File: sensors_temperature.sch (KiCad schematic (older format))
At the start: 3 parts

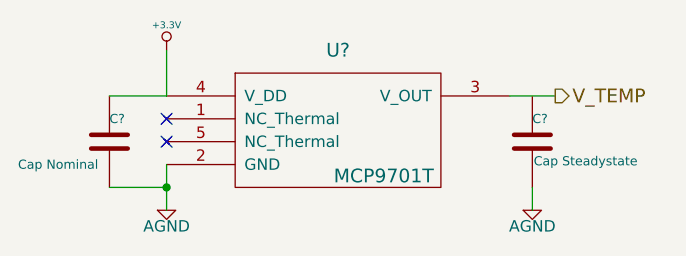
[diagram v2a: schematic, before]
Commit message: various fixes due to issues found in ERC
learned how to use invisible pins
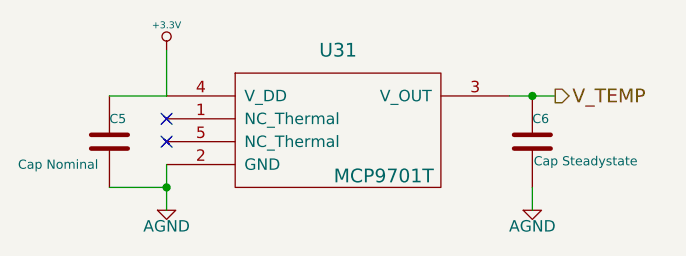
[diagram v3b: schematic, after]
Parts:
- gave numbers to parts that had none: 3
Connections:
- net V_TEMP: now also C6.1
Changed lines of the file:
@@
 $Descr A4 11693 8268
 encoding utf-8
-Sheet 9 18
+Sheet 7 18
 Title ""
-Date "18 dec 2013"
+Date "20 dec 2013"
 Rev ""
 Comp ""
@@
 $EndDescr
 $Comp
-L C C?
+L C C5
 U 1 1 5279CE8C
 P 1050 1250
-F 0 "C?" H 1050 1350 40  0000 L CNN
+F 0 "C5" H 1050 1350 40  0000 L CNN
 F 1 "Cap Nominal" H 650 1150 40  0000 L CNN
 F 2 "~" H 1088 1100 30  0000 C CNN
@@
 $EndComp
 $Comp
-L MCP9701T U?
+L MCP9701T U31
 U 1 1 5279CF6F
 P 2100 1250
-F 0 "U?" H 2050 1650 60  0000 C CNN
+F 0 "U31" H 2050 1650 60  0000 C CNN
 F 1 "MCP9701T" H 2250 1100 60  0000 C CNN
 F 2 "" H 1800 1650 60  0000 C CNN
@@
 $EndComp
 $Comp
-L +3.3V #PWR?
+L +3.3V #PWR039
 U 1 1 5279CF8D
 P 1300 850
-F 0 "#PWR?" H 1300 810 30  0001 C CNN
+F 0 "#PWR039" H 1300 810 30  0001 C CNN
 F 1 "+3.3V" H 1300 960 30  0000 C CNN
 F 2 "" H 1300 850 60  0000 C CNN
@@
 NoConn ~ 1300 1150
 NoConn ~ 1300 1250
-Wire Wire Line
-	2800 1050 3000 1050
 Connection ~ 1300 1450
 Wire Wire Line
@@
 	1300 1050 1050 1050
 Wire Wire Line
-	1300 1350 1300 1450
-Wire Wire Line
-	1300 1450 1300 1550
+	1300 1350 1300 1550
 Wire Wire Line
 	1300 850  1300 1050
@@
 	2900 1550 2900 1450
 $Comp
-L C C?
+L C C6
 U 1 1 527B2035
 P 2900 1250
-F 0 "C?" H 2900 1350 40  0000 L CNN
+F 0 "C6" H 2900 1350 40  0000 L CNN
 F 1 "Cap Steadystate" H 2906 1165 40  0000 L CNN
 F 2 "~" H 2938 1100 30  0000 C CNN
@@
 $EndComp
 $Comp
-L AGND #PWR?
+L AGND #PWR040
 U 1 1 527B2221
 P 1300 1550
-F 0 "#PWR?" H 1300 1550 40  0001 C CNN
+F 0 "#PWR040" H 1300 1550 40  0001 C CNN
 F 1 "AGND" H 1300 1480 50  0000 C CNN
 F 2 "" H 1300 1550 60  0000 C CNN
@@
 $EndComp
 $Comp
-L AGND #PWR?
+L AGND #PWR041
 U 1 1 527B2230
 P 2900 1550
-F 0 "#PWR?" H 2900 1550 40  0001 C CNN
+F 0 "#PWR041" H 2900 1550 40  0001 C CNN
 F 1 "AGND" H 2900 1480 50  0000 C CNN
 F 2 "" H 2900 1550 60  0000 C CNN
@@
 	1    0    0    -1
 $EndComp
+Wire Wire Line
+	2800 1050 3000 1050
+Connection ~ 2900 1050
 $EndSCHEMATC
